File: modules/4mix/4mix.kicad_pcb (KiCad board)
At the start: 4 copper layers, 91.4 x 68.6 mm, 168 parts, among them U1 MCP6002-xSN, U10 MCP6002-xSN, U11 MCP6002-xSN, U2 MCP6002-xSN, U3 MCP6002-xSN, U4 MCP6002-xSN, U5 MCP6002-xSN, U6 MCP6002-xSN, U7 MCP6002-xSN, U8 MCP6002-xSN, U9 MCP6002-xSN

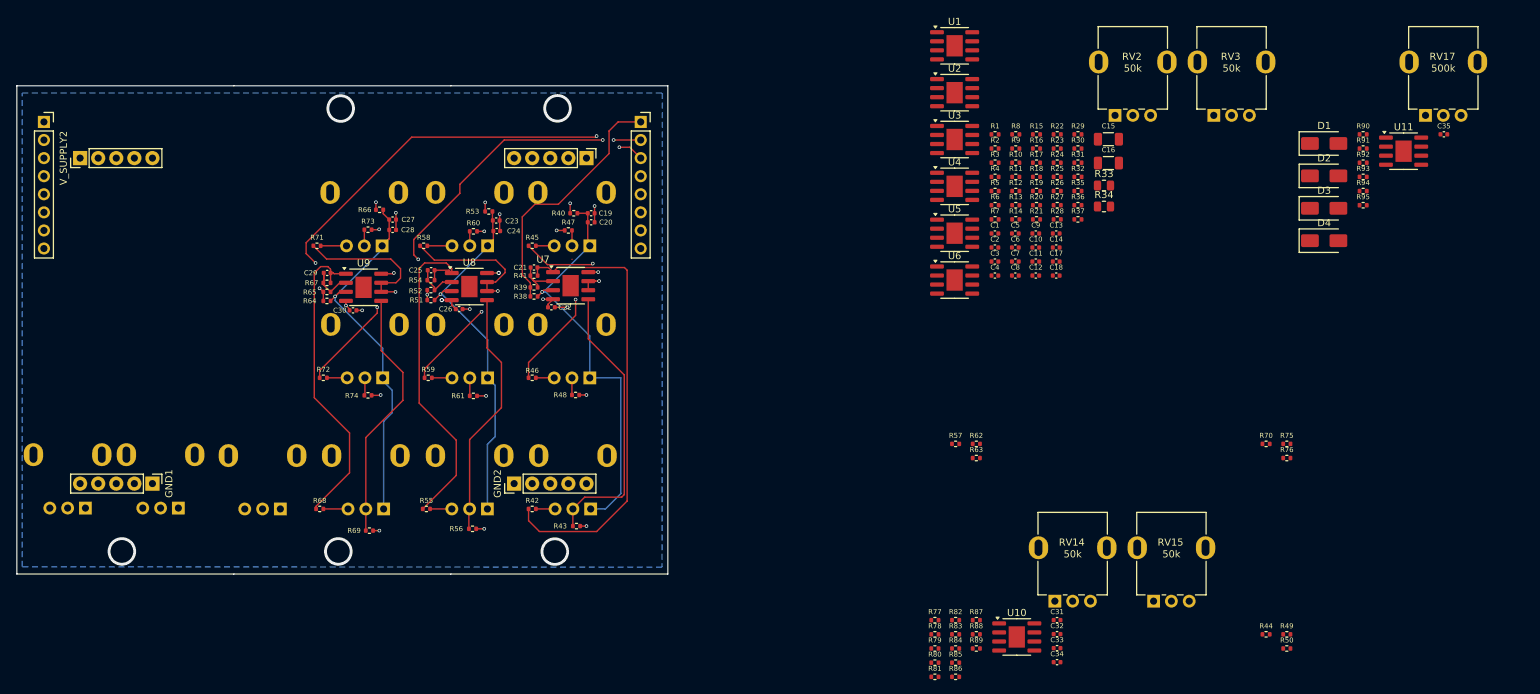
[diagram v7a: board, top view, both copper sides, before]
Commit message: Added channel 4
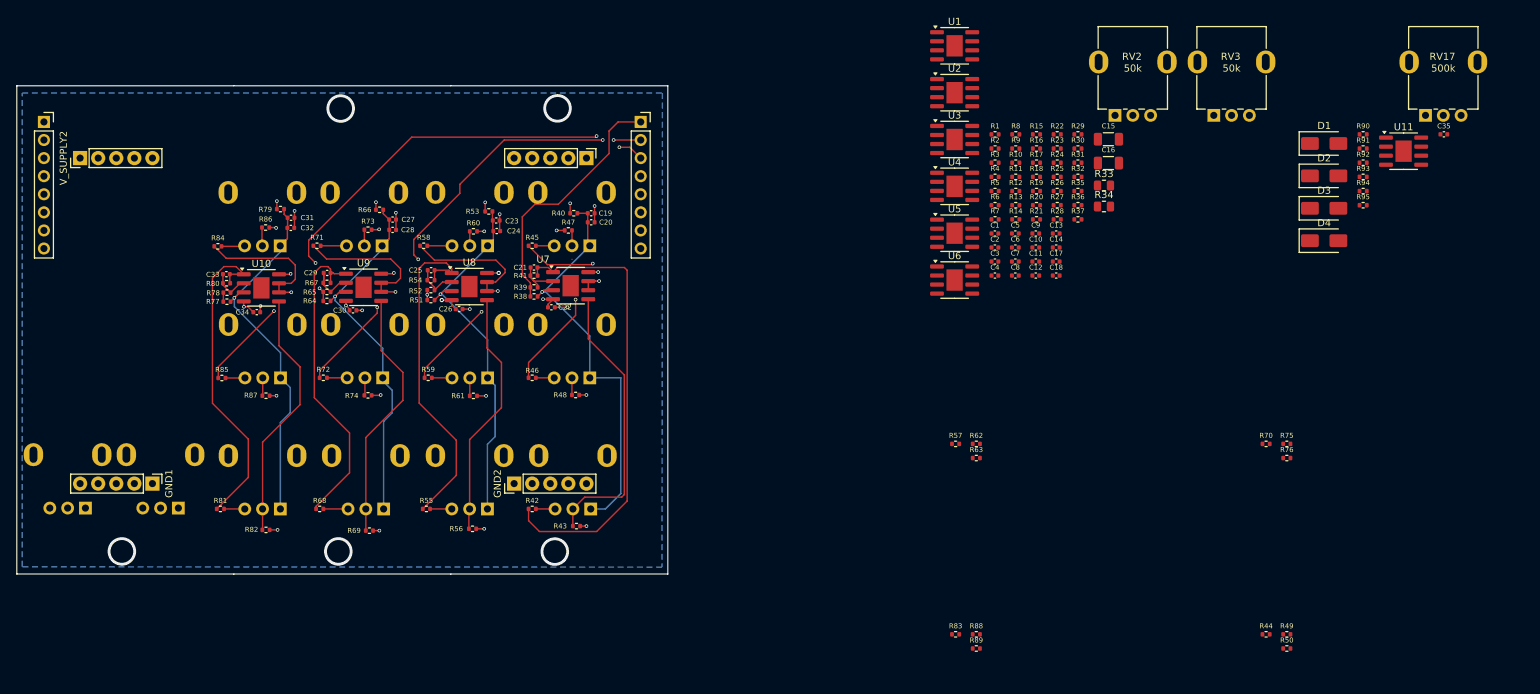
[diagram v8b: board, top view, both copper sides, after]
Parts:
- RV14, RV15: moved to B.Cu
- moved RV15 131.7 mm to (81.4, 74.7), turned to 180 degrees
- moved C33 128.0 mm to (76.4, 67.1)
- moved RV14 124.5 mm to (81.4, 56.1), turned to 180 degrees
- moved C34 122.7 mm to (80.7, 72.4), turned to 180 degrees
- moved C32 121.8 mm to (85.5, 60.6)
- moved C31 121.5 mm to (85.5, 59.2)
- moved R84 118.0 mm to (75.2, 63.2)
- moved U10 116.9 mm to (81.3, 69.0)
- moved R86 115.6 mm to (81.9, 60.6)
- moved R80 112.9 mm to (76.5, 68.4)
- moved R79 110.7 mm to (84.0, 58.0), turned to 180 degrees
- moved R85 110.5 mm to (75.8, 81.7)
- moved R78 110.4 mm to (76.5, 69.7)
- moved R77 109.0 mm to (76.5, 71.0), turned to 180 degrees
- moved R87 104.6 mm to (82.0, 84.2)
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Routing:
- net V_MID_4: track 0.00 -> 51.6 mm, vias 0 -> 1
- net Net-(C33-Pad2): track 0.00 -> 45.1 mm
- net Net-(U10B--): track 0.00 -> 36.3 mm, vias 0 -> 2
- net Net-(U10B-+): track 0.00 -> 35.5 mm
- net Net-(U10A--): track 0.00 -> 5.43 mm
- net GND: track 14.4 -> 19.2 mm, vias 6 -> 8
- net Net-(R84-Pad2): track 0.00 -> 3.27 mm
- net Net-(R81-Pad2): track 0.00 -> 2.91 mm
- net Net-(R85-Pad2): track 0.00 -> 2.74 mm
- net Net-(R86-Pad1): track 0.00 -> 2.60 mm
- net V_SUPPLY: track 8.49 -> 11.0 mm, vias 6 -> 8
- net Net-(R87-Pad1): track 0.00 -> 2.53 mm
- net IN_4: track 0.00 -> 1.27 mm
- net V_MID: track 3.74 -> 4.85 mm, vias 4 -> 5
- net Net-(R82-Pad2): track 0.00 -> 1.12 mm, vias 0 -> 1
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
